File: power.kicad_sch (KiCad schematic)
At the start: 31 parts, among them J13 FAN, Q1 AO3400A, SW1 SW_Push, SW2 SW_Push, U3 AMS1117-3.3

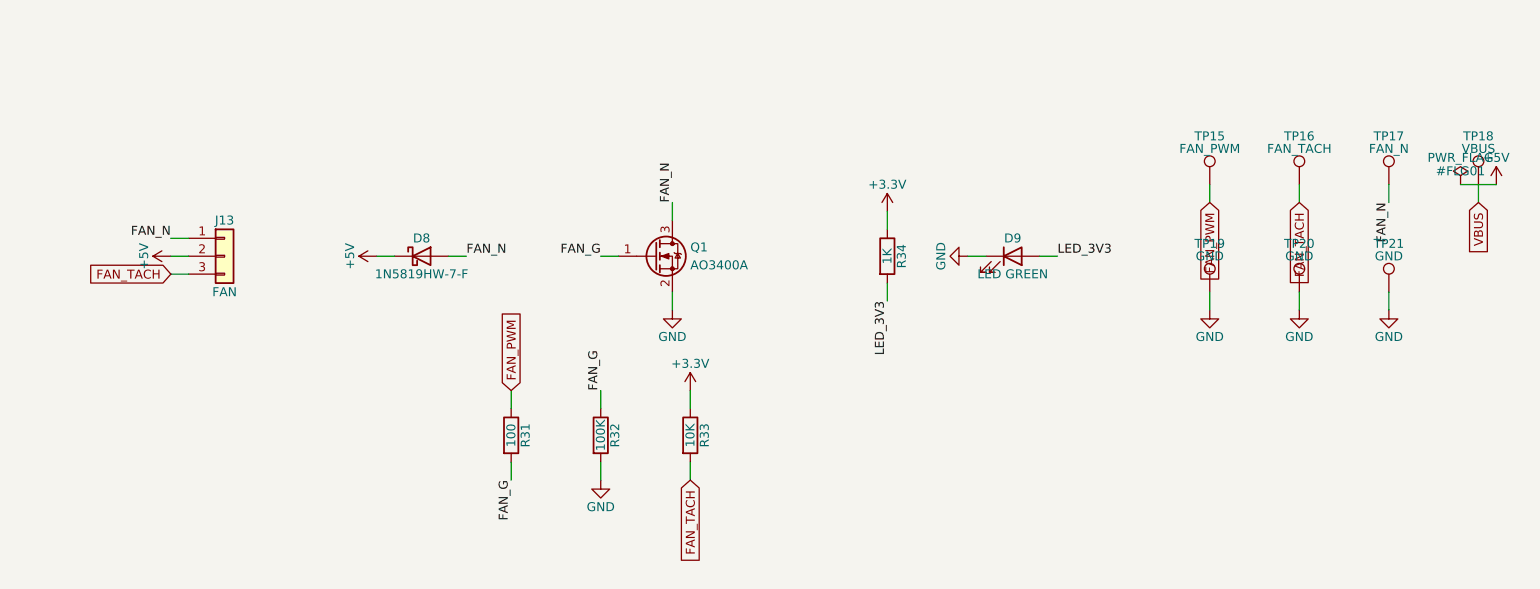
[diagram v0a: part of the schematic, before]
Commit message: Place decoupling caps, remove fan circuit and J3, add spare ESP32-Pi lines
Schematic:
- Remove the fan circuit (J13, Q1, D8, R31-R33, TP15-17); the Pi 5 drives
  its own Active Cooler. J1 pins 12/18 are now no-connect
- Remove the J3 debug header; J1 doubles as the dev header without a Pi
- IO0/IO1 to J1 pins 37/36 (Pi GPIO26/16) through R37/R38 1k as spare lines

Board:
- Test points moved to the bottom side to free space on top
- Decoupling caps C2/C3/C5/C8/C16/C18-C21 and R35/R36 placed next to
  their ICs; U8 nudged and R23/R10 moved to make room
- Conflicting tracks ripped up and rerouted; 6 connections left for
  interactive routing
- Back pinout table updated (fan and J3 rows replaced by J1 37/36)
- Courtyard exception rule for caps inside their IC's courtyard margin
- DRC (JLCPCB rules): 0 errors; ERC: 0 errors; schematic parity clean

Co-Authored-By: Claude Opus 5.5 <noreply@anthropic.com>
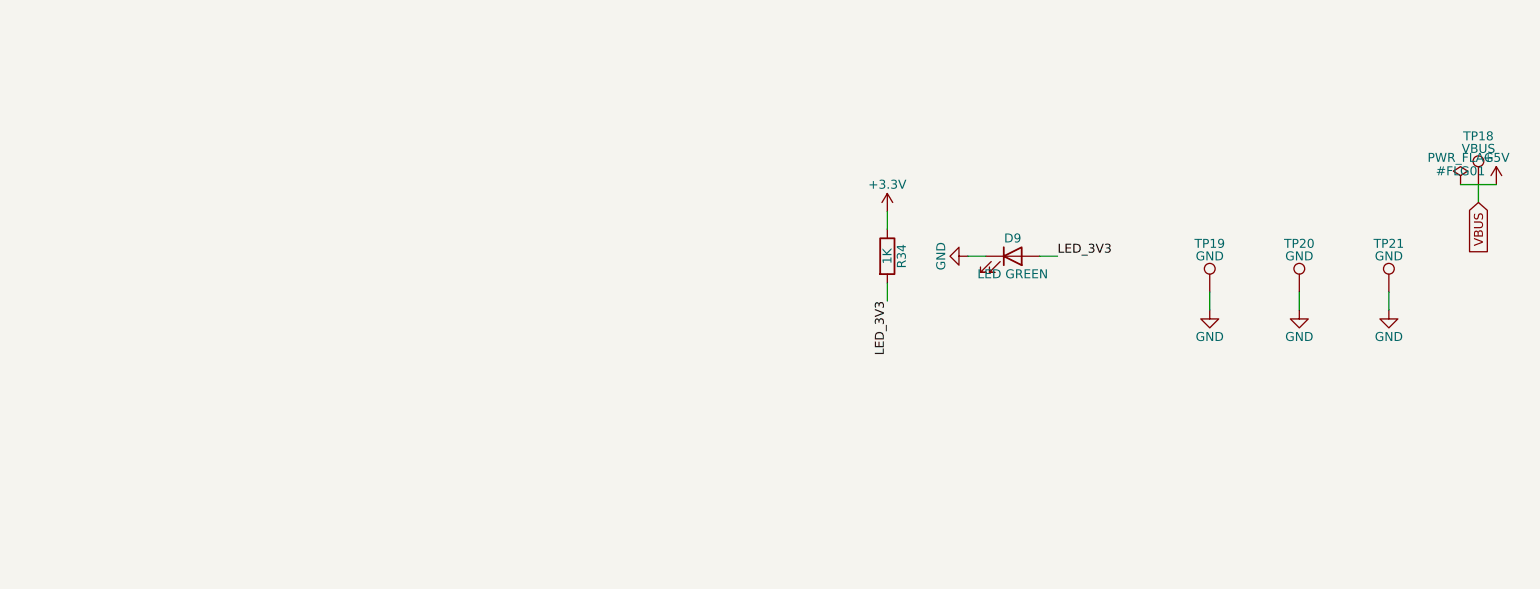
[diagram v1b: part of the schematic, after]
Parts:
- removed D8: 1N5819HW-7-F, Diode_SMD:D_SOD-123, symbol Device:D_Schottky
- removed J13: FAN, Connector_PinHeader_2.54mm:PinHeader_1x03_P2.54mm_Vertical, symbol Connector_Generic:Conn_01x03
- removed Q1: AO3400A, Package_TO_SOT_SMD:SOT-23, symbol Device:Q_NMOS_GSD
- removed R31: 100, Resistor_SMD:R_0603_1608Metric, symbol Device:R
- removed R32: 100K, Resistor_SMD:R_0603_1608Metric, symbol Device:R
- removed R33: 10K, Resistor_SMD:R_0603_1608Metric, symbol Device:R
- removed TP15: FAN_PWM, TestPoint:TestPoint_Pad_1.0x1.0mm, symbol Connector:TestPoint
- removed TP16: FAN_TACH, TestPoint:TestPoint_Pad_1.0x1.0mm, symbol Connector:TestPoint
- removed TP17: FAN_N, TestPoint:TestPoint_Pad_1.0x1.0mm, symbol Connector:TestPoint
